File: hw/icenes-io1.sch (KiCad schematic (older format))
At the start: 45 parts, among them U4 iCE40HX8K-CT256, U8 SN74LVC1404, U9 SN74LVC1404, Y1 21.47727MHz, Y2 26.601712MHz

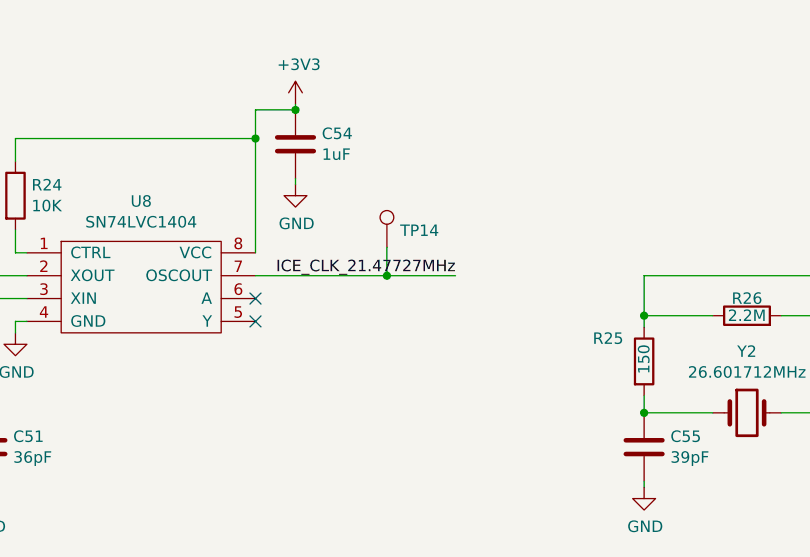
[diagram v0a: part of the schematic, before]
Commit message: Layout. Cleaned up nes connector footprints. Adjusted LED (D1) series resistor. Adjusted the voltage divider to BCBUS7 on FT2232H. Set pull up resistor to CDONE to 10k.
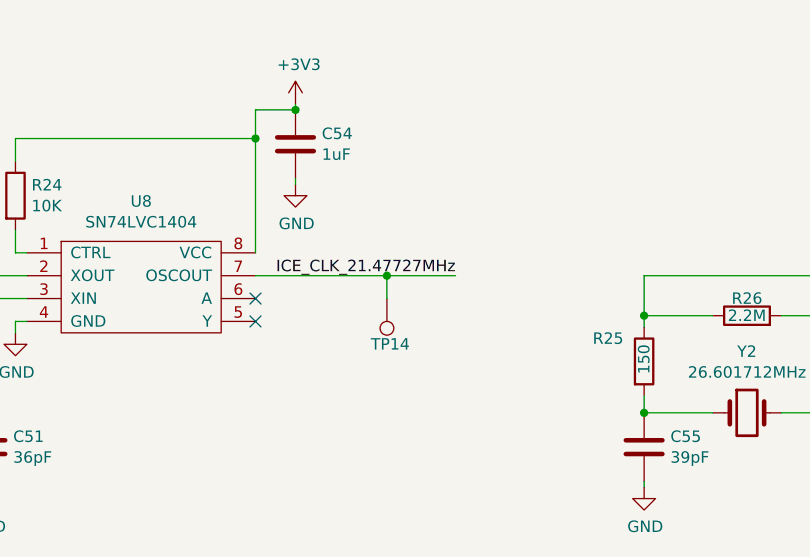
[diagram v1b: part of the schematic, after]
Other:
- moved on the sheet: TP14
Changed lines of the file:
@@
 ICE_CLK_21.47727MHz
-Wire Wire Line
-	3125 8850 3700 8850
 Wire Wire Line
 	2075 8650 2075 8750
@@
 	1    0    0    -1
 $EndComp
-Connection ~ 3700 8850
-Wire Wire Line
-	3700 8850 4000 8850
 $Comp
 L icenes-library:TestPoint TP14
 U 1 1 5DB07242
-P 3700 8725
-F 0 "TP14" H 3758 8797 50  0000 L CNN
-F 1 "TestPoint" H 3700 8925 50  0001 C CNN
-F 2 "TestPoint:TestPoint_Pad_D1.0mm" H 3900 8725 50  0001 C CNN
-F 3 "~" H 3900 8725 50  0001 C CNN
-	1    3700 8725
-	1    0    0    -1
-$EndComp
-Wire Wire Line
-	3700 8850 3700 8725
+P 3700 8950
+F 0 "TP14" H 3600 9150 50  0000 L CNN
+F 1 "TestPoint" H 3700 9150 50  0001 C CNN
+F 2 "TestPoint:TestPoint_Pad_D1.0mm" H 3900 8950 50  0001 C CNN
+F 3 "~" H 3900 8950 50  0001 C CNN
+	1    3700 8950
+	-1   0    0    1
+$EndComp
 $Comp
 L icenes-library:SN74LVC1404 U9
@@
 Text GLabel 4300 5400 2    50   Output ~ 0
 ICE_CPU_A11
+Wire Wire Line
+	3700 8950 3700 8850
+Wire Wire Line
+	3125 8850 3700 8850
+Wire Wire Line
+	3700 8850 4000 8850
+Connection ~ 3700 8850
 $EndSCHEMATC
